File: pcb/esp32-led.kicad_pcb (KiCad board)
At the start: 4 copper layers, 37.5 x 34 mm, 34 parts, among them IC1 ESP32-U4WDH, J1 USB_C_Receptacle_USB2.0, J2 Screw_Terminal_01x02, J3 Screw_Terminal_01x03, J4 JST-PH-4, Q1 MUN5211DW1, SW1 SW_Push, U1 AMS1117-3.3, U2 CP2102N-Axx-xQFN24

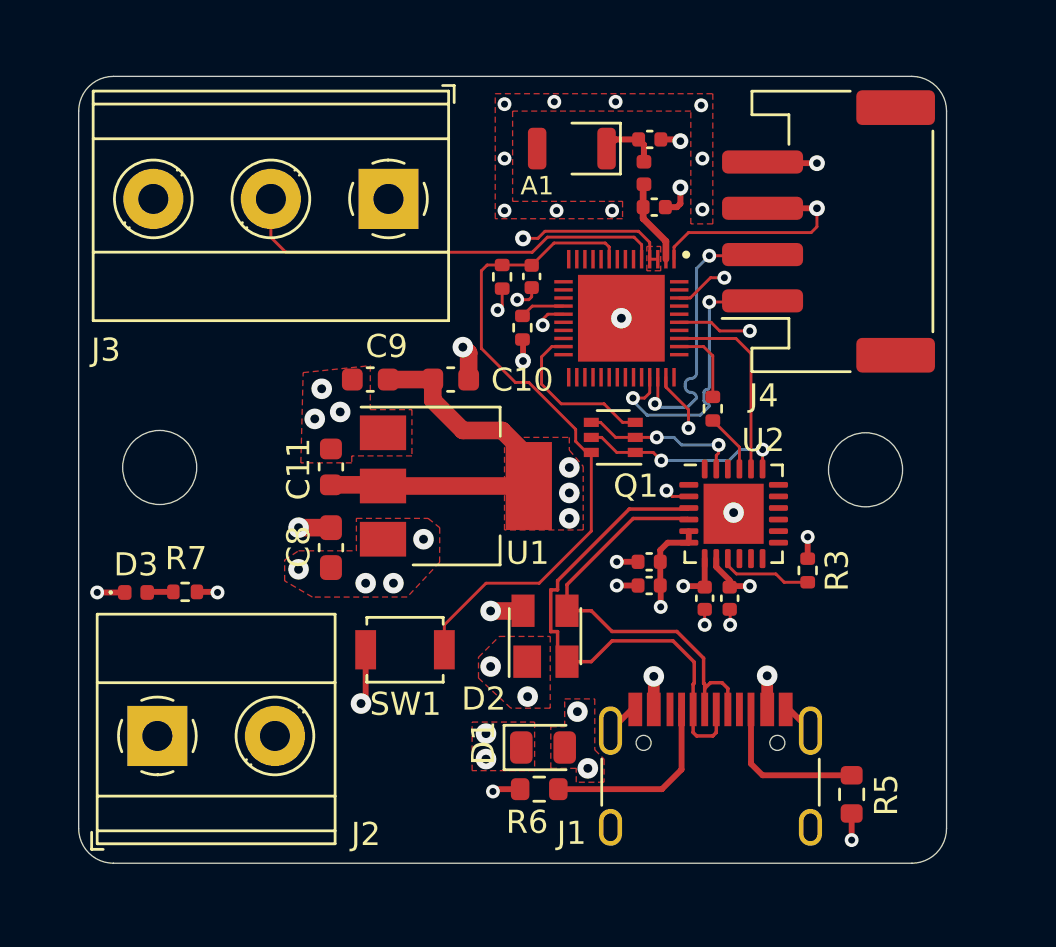
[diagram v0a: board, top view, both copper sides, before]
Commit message: ADD 3D Models for all footprints, export new PCB Image and remove D1 for R8 with 0R (Jumper R)
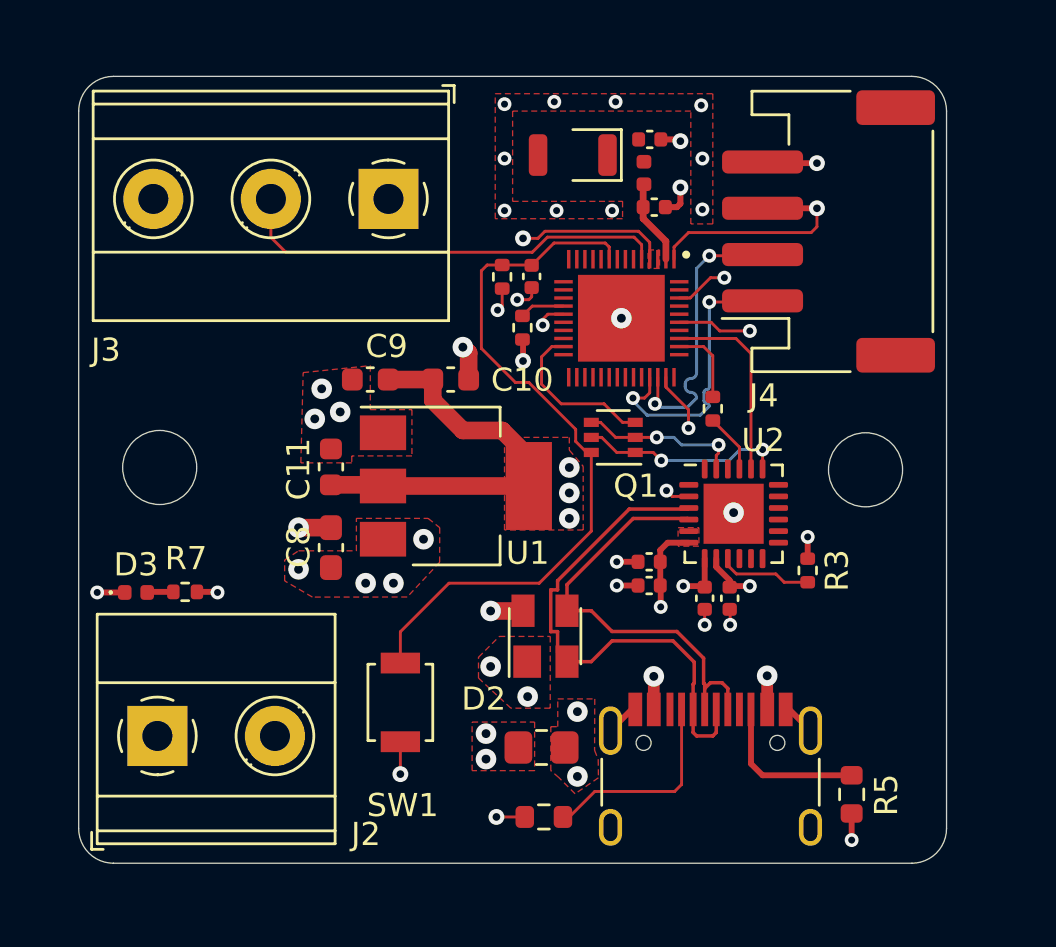
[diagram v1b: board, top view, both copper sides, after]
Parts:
- removed D1: D_Schottky, Diode_SMD:D_0805_2012Metric
- added R8: 0R, Resistor_SMD:R_0805_2012Metric_Pad1.20x1.40mm_HandSolder, F.Cu at (138.0, 103.0)
- A1: value YAGEO_ANT3216LL00R2300A -> YAGEO_ANT3216LL00R2400A; footprint RF_Antenna:YAGEO_ANT3216LL00R2300A -> RF_Antenna:YAGEO_ANT3216LL00R2400A
- moved SW1 2.28 mm to (131.9, 101.0), turned to -90 degrees
- moved R6 1.22 mm to (138.1, 106.0)
- moved A1 0.28 mm to (139.3, 77.4)
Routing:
- net Net-(A1-Pad1): track 2.64 -> 0.03 mm
- net EN: track 29.5 -> 31.8 mm
- net GND: track 22.7 -> 21.7 mm
- net +3.3VA: track 55.1 -> 54.2 mm
- net Net-(J1-PadA5): track 8.27 -> 8.95 mm

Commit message: ADD new picture, and propper GND plane on top layer
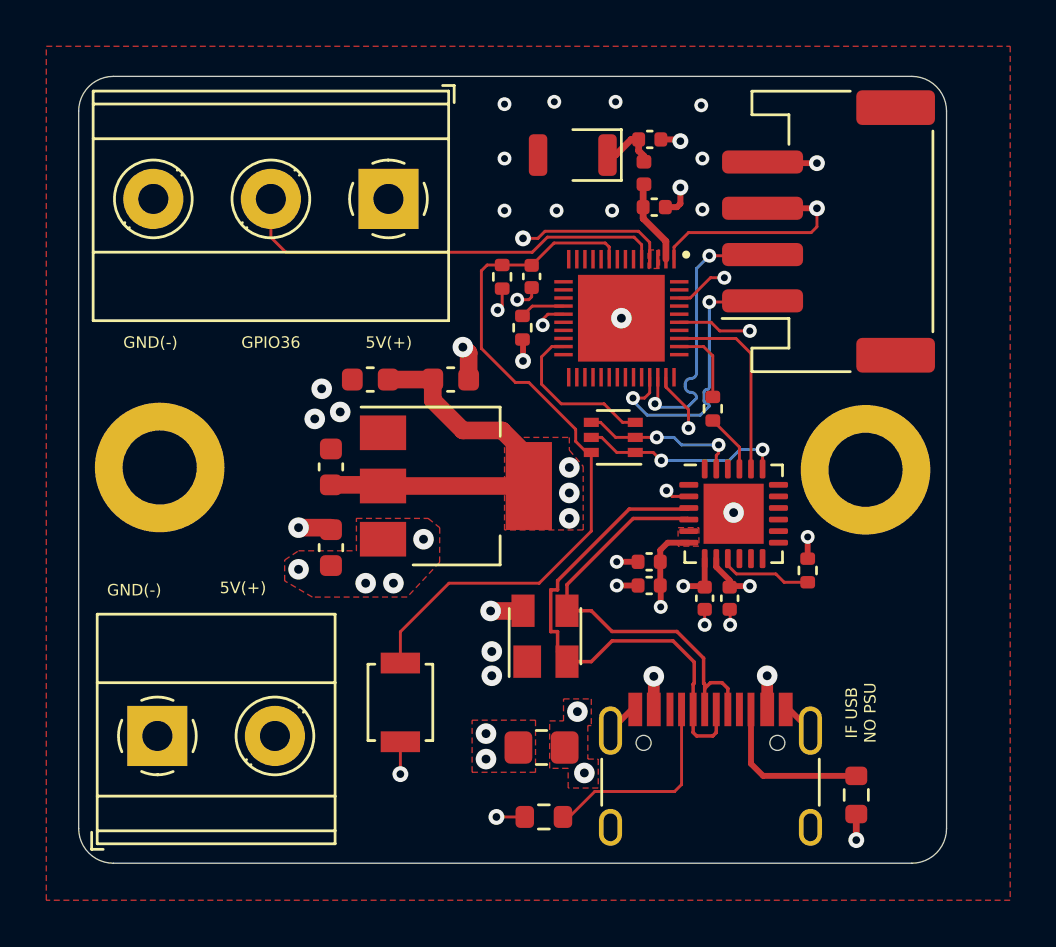
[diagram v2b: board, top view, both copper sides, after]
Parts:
- removed D3: LED, LED_SMD:LED_0402_1005Metric
- removed R7: 200, Resistor_SMD:R_0402_1005Metric
- C10: value 10uF/6.3V(10%) -> 10uF
- C11: value 0.1uF/25V(10%) -> 100nF
- C3: value 10uF -> 100nF
- C6, C7: value 0.1uF -> 100nF
- C8: footprint Capacitor_SMD:C_0603_1608Metric_Pad1.08x0.95mm_HandSolder -> Capacitor_SMD:C_0603_1608Metric
- H1, H2: value MountingHole -> MountingHole_Pad; footprint MountingHole:MountingHole_3.2mm_M3_DIN965 -> MountingHole:MountingHole_3.2mm_M3_DIN965_Pad
- R1: value 10K -> 100k
- R3: value 2K -> 2k
- moved R5 0.20 mm to (151.6, 105.0)
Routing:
- net Net-(A1-Pad1): track 0.03 -> 2.68 mm
- net GND: track 21.7 -> 20.5 mm, vias 33 -> 32
- net Net-(D3-Pad2): track 1.14 -> 0.00 mm
- net HIGH_POWER_5V: track 2.30 -> 1.40 mm, vias 8 -> 7
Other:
- board text added: "5V(+)"
- board text added: "Designed by Tim Schmid"
- board text added: "GND(-)"
- board text added: "GPIO36"
- board text added: "IF USB NO PSU"
- board text added: "Ref 1.0"
- board text added: "Tiny ESP32 LED driver"

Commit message: UPDATE thermal relief pads for ESP, USB-UART
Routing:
- net GND: vias 32 -> 30

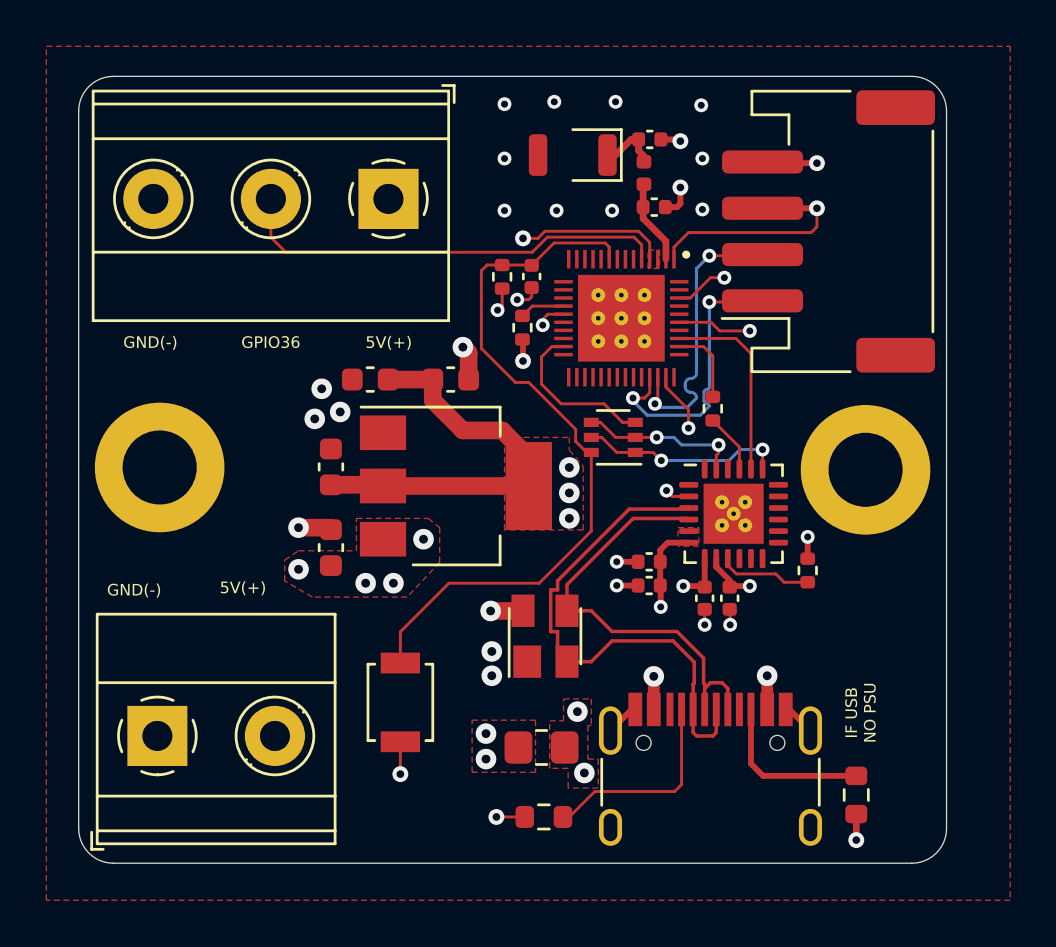
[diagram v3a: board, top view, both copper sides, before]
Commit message: REF PCB Layout, Switch to new USB-C Receptable
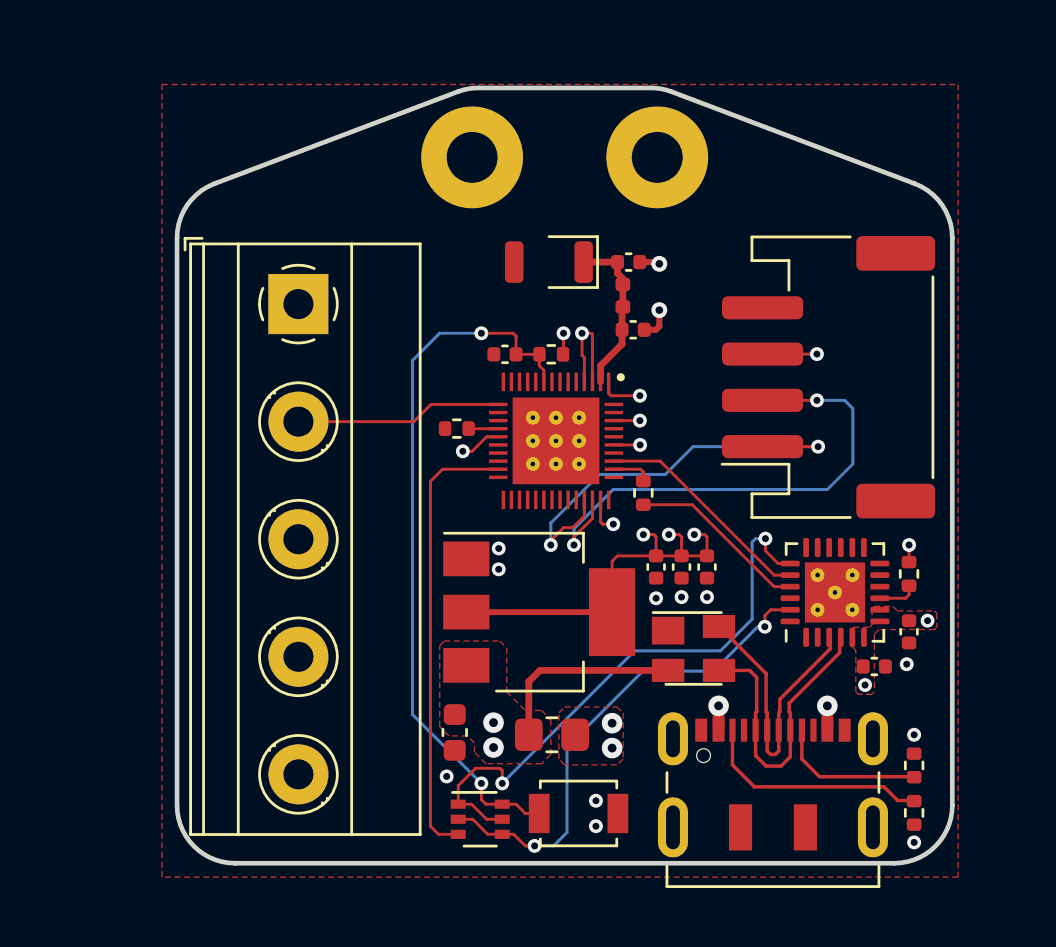
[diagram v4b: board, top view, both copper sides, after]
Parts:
- removed the C5 at (146.1, 96.5)
- removed the C7 at (142.7, 95.0)
- removed D2: SP0503BAHT, Package_TO_SOT_SMD:SOT-143
- removed J4: JST-PH-4, Connector_JST:JST_PH_S4B-PH-SM4-TB_1x04-1MP_P2.00mm_Horizontal
- removed R8: 0R, Resistor_SMD:R_0805_2012Metric_Pad1.20x1.40mm_HandSolder
- removed the U1 at (134.3, 91.7)
- added D1: SP0503BAHT, Package_TO_SOT_SMD:SOT-143, F.Cu at (144.6, 98.7)
- added R7: 5.11K, Resistor_SMD:R_0402_1005Metric, F.Cu at (154.1, 105.8)
- added U2: AMS1117-3.3, Package_TO_SOT_SMD:SOT-223-3_TabPin2, F.Cu at (137.9, 97.2)
- C1: value 8pF -> 8p
- C2: value 10pF -> 10p
- C3: value 100nF -> 100n
- C4: value 4.7uF -> 4.7u
- C5: renamed from C6; value 100nF -> 10n
- C6: renamed from C8; value 10uF -> 10u
- C7: renamed from C9; value 10uF -> 10u; footprint Capacitor_SMD:C_0603_1608Metric -> Capacitor_SMD:C_0402_1005Metric
- C8: renamed from C10; value 10uF -> 4.7u; footprint Capacitor_SMD:C_0603_1608Metric -> Capacitor_SMD:C_0402_1005Metric
- C9: renamed from C11; value 100nF -> 100n; footprint Capacitor_SMD:C_0603_1608Metric -> Capacitor_SMD:C_0402_1005Metric
- H1, H2: footprint MountingHole:MountingHole_3.2mm_M3_DIN965_Pad -> MountingHole:MountingHole_2.2mm_M2_Pad
- J1: footprint Connector_USB:USB_C_Receptacle_HRO_TYPE-C-31-M-12 -> Connector_USB:USB_C_Receptacle_JAE_DX07S016JA1R1500
- J2: value Screw_Terminal_01x02 -> Screw_Terminal_01x05; footprint TerminalBlock_Phoenix:TerminalBlock_Phoenix_MKDS-1,5-2-5.08_1x02_P5.08mm_Horizontal -> TerminalBlock_Phoenix:TerminalBlock_Phoenix_MKDS-1,5-5-5.08_1x05_P5.08mm_Horizontal
- J3: value Screw_Terminal_01x03 -> JST-PH-4; footprint TerminalBlock_Phoenix:TerminalBlock_Phoenix_MKDS-1,5-3-5.08_1x03_P5.08mm_Horizontal -> Connector_JST:JST_PH_S4B-PH-SM4-TB_1x04-1MP_P2.00mm_Horizontal
- L1: value 1nH -> 1n
- R2: value 10K(5%) -> 100k
- R3: value 2k -> 1k
- R4: value 499R(1%) -> 499R
- R5: value 5.11K -> 0R; footprint Resistor_SMD:R_0603_1608Metric -> Resistor_SMD:R_0805_2012Metric_Pad1.20x1.40mm_HandSolder
- R6: value 5.11K -> 5.11k; footprint Resistor_SMD:R_0603_1608Metric -> Resistor_SMD:R_0402_1005Metric
- moved J3 20.5 mm to (150.4, 87.0), turned to 90 degrees
- moved J2 19.6 mm to (127.5, 83.8), turned to -90 degrees
- moved H1 19.0 mm to (135.0, 77.5)
- moved Q1 17.5 mm to (135.3, 106.1), turned to 0 degrees
- moved C9 16.8 mm to (145.2, 95.2), turned to -90 degrees
- moved H2 16.2 mm to (143.0, 77.5)
- moved R6 16.2 mm to (154.1, 103.8), turned to 90 degrees
- moved C7 14.8 mm to (142.9, 95.2), turned to -90 degrees
- moved R5 13.4 mm to (138.4, 102.5), turned to 180 degrees
- moved C8 12.8 mm to (144.1, 95.2), turned to -90 degrees
- moved C5 10.3 mm to (152.4, 99.5), turned to 0 degrees
- moved C6 9.61 mm to (134.2, 102.3), turned to -90 degrees
- moved SW1 9.07 mm to (139.6, 105.8), turned to 0 degrees
- moved C4 8.95 mm to (153.9, 98.0)
- moved IC1 6.00 mm to (138.6, 89.8)
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- renumbered U2 to U1
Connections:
- net Net-(IC1-Pad18) renamed /ESP32-U4WDH/MTDI
- net Net-(R3-Pad2) renamed /USB to UART /RST
- net Net-(R4-Pad1) renamed /USB to UART /TXD
- A1 pad 1: Net-(A1-Pad1) -> /ESP32-U4WDH/ANTENNA
- C1 pad 1: Net-(A1-Pad1) -> /ESP32-U4WDH/ANTENNA
- C4 pad 1: +3.3VA -> +3V3
- C5 pad 1: +3.3VA -> +3V3
- C6 pad 1: HIGH_POWER_5V -> +5V
- C7 pad 1: +3.3VA -> +3V3
- C8 pad 1: +3.3VA -> +3V3
- C9 pad 1: +3.3VA -> +3V3
- IC1 pad 1: +3.3VA -> +3V3
- IC1 pad 15: unconnected-(IC1-Pad15) -> GPIO26
- IC1 pad 19: +3.3VA -> +3V3
- IC1 pad 3: +3.3VA -> +3V3
- IC1 pad 37: +3.3VA -> +3V3
- IC1 pad 4: +3.3VA -> +3V3
- IC1 pad 43: +3.3VA -> +3V3
- IC1 pad 46: +3.3VA -> +3V3
- IC1 pad 5: GPIO36 -> unconnected-(IC1-Pad5)
- J1 pad A4: Net-(J1-PadA4) -> /5V to 3.3V Power/VBUS
- J1 pad A5: Net-(J1-PadA5) -> /5V to 3.3V Power/CC1
- J1 pad A6: D- -> D+
- J1 pad A7: D+ -> D-
- J1 pad A9: Net-(J1-PadA4) -> /5V to 3.3V Power/VBUS
- J1 pad B4: Net-(J1-PadA4) -> /5V to 3.3V Power/VBUS
- J1 pad B5: Net-(J1-PadB5) -> /5V to 3.3V Power/CC2
- J1 pad B6: D- -> D+
- J1 pad B7: D+ -> D-
- J1 pad B9: Net-(J1-PadA4) -> /5V to 3.3V Power/VBUS
- J2 pad 1: GND -> +5V
- J2 pad 2: HIGH_POWER_5V -> GPIO26
- J3 pad 1: HIGH_POWER_5V -> SCL
- J3 pad 2: GPIO36 -> SDA
- J3 pad 3: GND -> +3V3
- L1 pad 1: Net-(A1-Pad1) -> /ESP32-U4WDH/ANTENNA
- R1 pad 1: +3.3VA -> +3V3
- R3 pad 1: +3.3VA -> +3V3
- R5 pad 1: Net-(J1-PadB5) -> /5V to 3.3V Power/VBUS
- R5 pad 2: GND -> +5V
- R6 pad 1: Net-(J1-PadA5) -> /5V to 3.3V Power/CC2
- U1 pad 5: +3.3VA -> +3V3
- U1 pad 6: +3.3VA -> +3V3
- U1 pad 7: +3.3VA -> +3V3
- U1 pad 8: +3.3VA -> +3V3
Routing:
- net +3.3VA: track 54.2 -> 0.00 mm, vias 14 -> 0
- net +3V3: track 0.00 -> 33.1 mm, vias 0 -> 14
- net GPIO36: track 19.0 -> 0.00 mm
- net GND: track 20.5 -> 2.29 mm, vias 30 -> 13
- net /USB to UART /RTS: track 8.85 -> 25.3 mm
- net /USB to UART /DTR: track 6.98 -> 21.5 mm
- net GPIO0: track 7.05 -> 19.4 mm
- net SDA: track 12.5 -> 22.6 mm
- net /5V to 3.3V Power/CC1: track 0.00 -> 9.99 mm
- net D+: track 22.7 -> 12.7 mm
- net Net-(J1-PadA5): track 8.95 -> 0.00 mm
- net GPIO26: track 0.00 -> 8.94 mm
- net +5V: track 0.00 -> 8.52 mm, vias 0 -> 2
- net Net-(J1-PadB5): track 7.11 -> 0.00 mm
- net SCL: track 12.4 -> 19.1 mm
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- added copper zone on F.Cu, net +3V3
- added copper zone on In2.Cu, net +3V3
- added copper zone on F.Cu, net +5V
- added copper zone on In2.Cu, net +5V
- added copper zone on F.Cu, net /5V to 3.3V Power/VBUS
- added copper zone on In2.Cu, net /5V to 3.3V Power/VBUS
- removed copper zone on F.Cu, net +3.3VA
- removed copper zone on In2.Cu, net +3.3VA
- removed copper zone on F.Cu, net HIGH_POWER_5V
- removed copper zone on In2.Cu, net HIGH_POWER_5V
- removed copper zone on F.Cu, net Net-(J1-PadA4)
- removed copper zone on In2.Cu, net Net-(J1-PadA4)
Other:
- board size 37.5 x 34 mm -> 33.5 x 33.5 mm
- rule pad_to_mask_clearance: 0 -> 0.05
- board text added: "Digital LED-Strip"
- board text added: "External Power-Supply"
- board text added: "GPIO26"
- board text removed: "GPIO36"
- board text removed: "IF USB NO PSU"

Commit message: REF TVS-Diode Layout
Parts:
- moved D1 0.86 mm to (145.4, 98.5), turned to -90 degrees
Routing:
- net +5V: track 8.52 -> 11.6 mm
- net /5V to 3.3V Power/VBUS: track 2.10 -> 5.04 mm
- net /USB to UART /DTR: track 21.5 -> 22.3 mm
- net D+: track 12.7 -> 12.0 mm
- net D-: track 13.1 -> 13.6 mm
